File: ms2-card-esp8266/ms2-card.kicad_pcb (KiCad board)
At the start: 2 copper layers, 100 x 54 mm, 56 parts, among them J1 Schaltregler, J10 MicroSD_SPI_CD, J11 Conn_01x06, J2 ESP Prog, J20 Smartcard Connector, J21 PogoPin, J22 Card Edge, J23 Conn_01x04, J30 USB_B_Micro, J31 Power Select, J32 Conn_01x03, Q1 MMBT3904, Q2 MMBT3904, SW1 RESET, U1 ESP-12F, U2 FM24C64B, U20 BL1551B, U3 BL1551B, U30 CP2102N-Axx-xQFN24, U4 BL1551B, U6 AMS1117-3.3

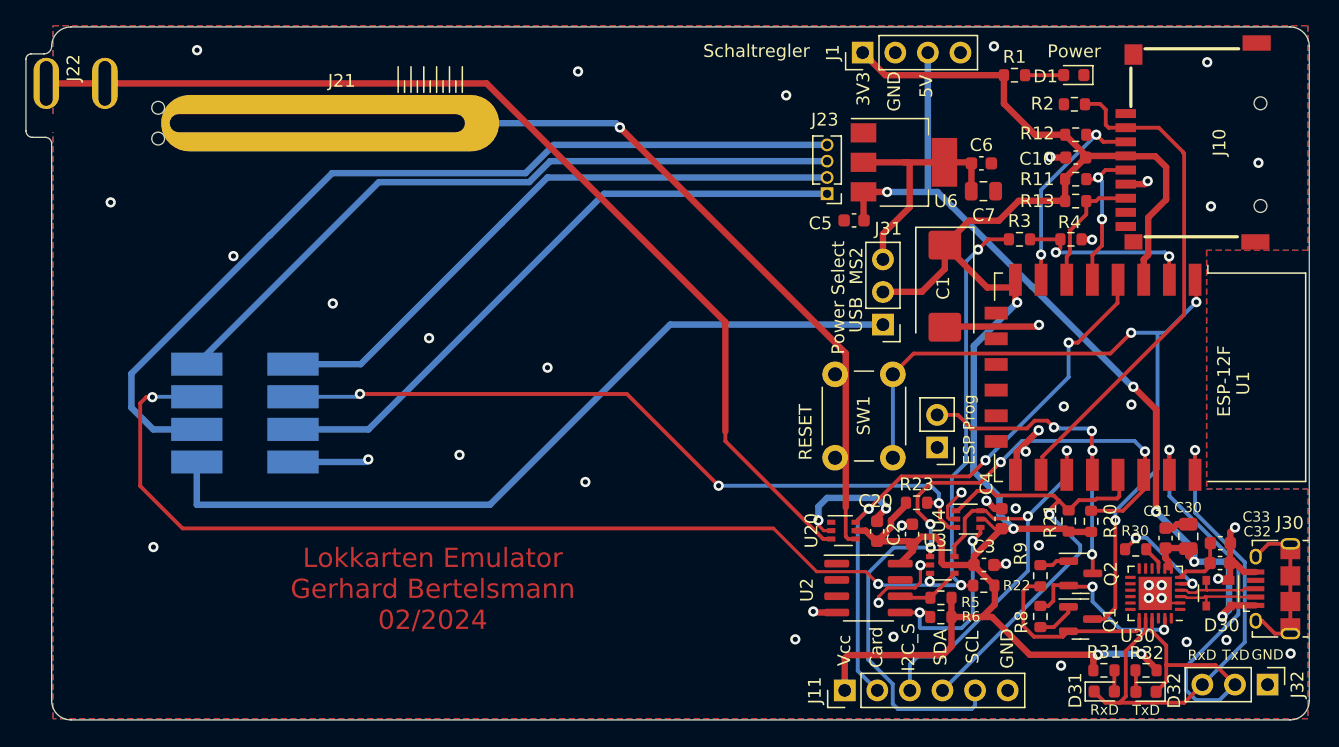
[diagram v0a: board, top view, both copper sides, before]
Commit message: add RC ADC oart
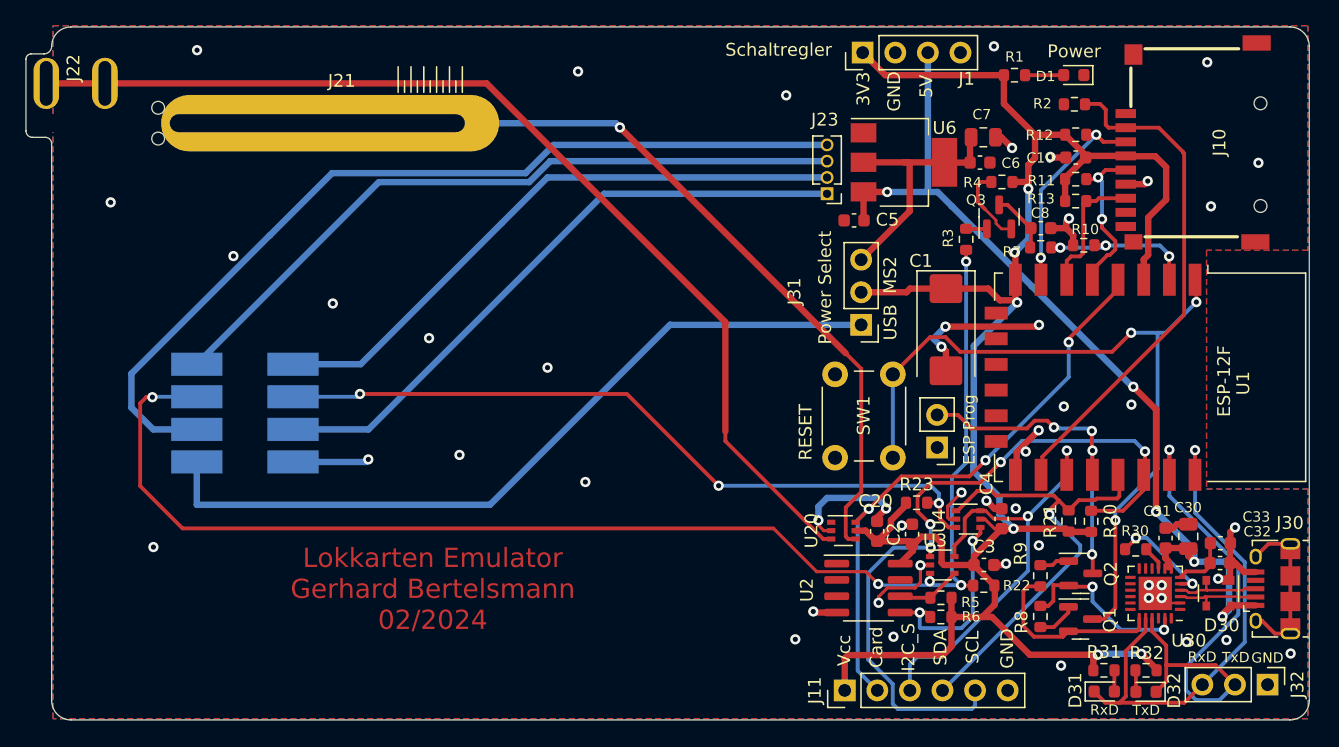
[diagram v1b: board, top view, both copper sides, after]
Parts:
- added C8: 470nF, Capacitor_SMD:C_0603_1608Metric, F.Cu at (177.1, 115.7)
- added Q3: MMBT5401, Package_TO_SOT_SMD:SOT-23, F.Cu at (173.8, 114.8)
- added R10: 75k, Resistor_SMD:R_0603_1608Metric, F.Cu at (180.4, 117.0)
- added R7: 180k, Resistor_SMD:R_0603_1608Metric, F.Cu at (177.1, 117.2)
- R3: value 220K -> 10k
- R4: value 100K -> 100
- moved R4 6.99 mm to (174.1, 112.1), turned to 0 degrees
- moved C7 4.20 mm to (172.6, 108.6)
- moved R3 4.16 mm to (171.3, 116.5), turned to -90 degrees
- moved C1 3.39 mm to (169.7, 123.6)
- moved J31 1.70 mm to (163.1, 123.2)
- moved C6 0.13 mm to (172.3, 110.6)
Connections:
- R3 pad 1: /CSCL -> Net-(Q3-Pad1)
- R3 pad 2: Net-(U1-Pad2) -> /CSCL
- R4 pad 1: GND -> Net-(Q3-Pad2)
- R4 pad 2: Net-(U1-Pad2) -> VCC
- U1 pad 2: Net-(U1-Pad2) -> /ADC
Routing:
- net Net-(U1-Pad2): track 14.3 -> 0.00 mm, vias 2 -> 0
- net /ADC: track 0.00 -> 12.4 mm, vias 0 -> 3
- net GND: track 56.9 -> 65.4 mm, vias 47 -> 50
- net Net-(Q3-Pad2): track 0.00 -> 6.11 mm
- net Net-(C8-Pad1): track 0.00 -> 4.75 mm
- net /CSCL: track 110.2 -> 107.1 mm
- net /MS2PWR: track 62.6 -> 60.9 mm
- net Net-(Q3-Pad1): track 0.00 -> 1.63 mm
- net /PP: track 63.7 -> 64.7 mm
- net /CLK: track 11.8 -> 12.8 mm
- net VCC: track 158.9 -> 159.9 mm, vias 4 -> 6
- net /nRST: track 59.3 -> 60.2 mm

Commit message: some small fixes
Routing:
- net GND: vias 50 -> 63
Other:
- board text added: "Lokkarten Emulator Gerhard Bertelsmann 03/2024"
- board text removed: "Lokkarten Emulator Gerhard Bertelsmann 02/2024"
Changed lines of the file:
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@@
   (title_block
     (title "Lokkkarten Emulator")
-    (date "2024-02-22")
-    (rev "0.96")
+    (date "2024-02-25")
+    (rev "0.98")
     (comment 1 "Gerhard Bertelsmann")
   )
@@
     (property "Sheetname" "")
     (attr smd)
-    (fp_text reference "C2" (at 0 -1.43 90) (layer "F.SilkS")
-      (effects (font (size 1 1) (thickness 0.15)))
+    (fp_text reference "C2" (at -0.545 -1.24 90) (layer "F.SilkS")
+      (effects (font (size 0.8 0.8) (thickness 0.15)))
     )
     (fp_text value "100nF" (at 0 1.43 90) (layer "F.Fab") hide
@@
     (property "Sheetname" "")
     (attr smd)
-    (fp_text reference "C20" (at 2.35 -0.125 180) (layer "F.SilkS")
-      (effects (font (size 1 1) (thickness 0.15)))
+    (fp_text reference "C20" (at 2.59 0.055 270) (layer "F.SilkS")
+      (effects (font (size 0.8 0.8) (thickness 0.15)))
     )
     (fp_text value "100nF" (at 0 1.43 90) (layer "F.Fab") hide
@@
     (property "Sheetname" "")
     (attr smd)
-    (fp_text reference "U3" (at -0.56 -1.905 180) (layer "F.SilkS")
-      (effects (font (size 1 1) (thickness 0.15)))
+    (fp_text reference "U3" (at -0.55 -2.015 180) (layer "F.SilkS")
+      (effects (font (size 0.8 0.8) (thickness 0.15)))
     )
     (fp_text value "BL1551B" (at 2.75 0 90) (layer "F.Fab") hide
@@
     (property "Sheetname" "")
     (attr smd)
-    (fp_text reference "U4" (at -2.275 0.14 90) (layer "F.SilkS")
-      (effects (font (size 1 1) (thickness 0.15)))
+    (fp_text reference "U4" (at 0.435 -1.86 180) (layer "F.SilkS")
+      (effects (font (size 0.8 0.8) (thickness 0.15)))
     )
     (fp_text value "BL1551B" (at 0 2 180) (layer "F.Fab") hide
@@
     (property "Sheetname" "")
     (attr smd)
-    (fp_text reference "C4" (at 2.745 -1.175 90) (layer "F.SilkS")
-      (effects (font (size 1 1) (thickness 0.15)))
+    (fp_text reference "C4" (at -0.015 1.525 90) (layer "F.SilkS")
+      (effects (font (size 0.8 0.8) (thickness 0.15)))
     )
     (fp_text value "100nF" (at 0 1.43 90) (layer "F.Fab") hide
@@
     (property "Sheetname" "")
     (attr smd)
-    (fp_text reference "C3" (at 0 -1.43) (layer "F.SilkS")
-      (effects (font (size 1 1) (thickness 0.15)))
+    (fp_text reference "C3" (at 0.15 -1.245) (layer "F.SilkS")
+      (effects (font (size 0.8 0.8) (thickness 0.15)))
     )
     (fp_text value "100nF" (at 0 1.43) (layer "F.Fab") hide
@@
   (gr_arc (start 100 101.5) (mid 100.43934 100.43934) (end 101.5 100) (layer "Edge.Cuts") (width 0.05))
   (gr_arc (start 196.5 100) (mid 197.56066 100.43934) (end 198 101.5) (layer "Edge.Cuts") (width 0.05))
-  (gr_text "Lokkarten Emulator\nGerhard Bertelsmann\n02/2024" (at 129.7 143.8) (layer "F.Cu")
+  (gr_text "Lokkarten Emulator\nGerhard Bertelsmann\n03/2024" (at 129.7 143.8) (layer "F.Cu")
     (effects (font (size 1.5 1.5) (thickness 0.3)))
   )
-  (gr_text "SCL" (at 171.76 148.34 90) (layer "F.SilkS")
+  (gr_text "SCL" (at 172.07 148.71 90) (layer "F.SilkS")
     (effects (font (size 1 1) (thickness 0.15)))
   )
-  (gr_text "GND" (at 174.46 148.44 90) (layer "F.SilkS")
+  (gr_text "GND" (at 174.53 148.63 90) (layer "F.SilkS")
     (effects (font (size 1 1) (thickness 0.15)))
   )
@@
     (effects (font (size 1 1) (thickness 0.15)))
   )
-  (gr_text "Vcc" (at 161.76 148.59 90) (layer "F.SilkS")
+  (gr_text "Vcc" (at 161.83 148.94 90) (layer "F.SilkS")
     (effects (font (size 1 1) (thickness 0.15)))
   )
@@
     (effects (font (size 0.8 0.8) (thickness 0.15)))
   )
-  (gr_text "SDA" (at 169.26 148.34 90) (layer "F.SilkS")
+  (gr_text "SDA" (at 169.49 148.77 90) (layer "F.SilkS")
     (effects (font (size 1 1) (thickness 0.15)))
   )
@@
     (effects (font (size 0.8 0.8) (thickness 0.15)))
   )
-  (gr_text "I2C_S" (at 166.76 148.34 90) (layer "F.SilkS")
+  (gr_text "I2C_S" (at 166.94 148.35 90) (layer "F.SilkS")
     (effects (font (size 1 1) (thickness 0.15)))
   )
-  (gr_text "Card" (at 164.26 148.34 90) (layer "F.SilkS")
+  (gr_text "Card" (at 164.4 148.51 90) (layer "F.SilkS")
     (effects (font (size 1 1) (thickness 0.15)))
   )
@@
   (segment (start 160.175 139.25) (end 159.75 138.825) (width 0.25) (layer "F.Cu") (net 2))
   (segment (start 179.605 116.225) (end 179.605 117.01) (width 0.5) (layer "F.Cu") (net 2))
-  (via (at 185.5 143.5) (size 0.8) (drill 0.4) (layers "F.Cu" "B.Cu") (net 2))
+  (via (at 185.41 143.55) (size 0.8) (drill 0.4) (layers "F.Cu" "B.Cu") (net 2))
+  (via (at 183.29 104.5) (size 0.8) (drill 0.4) (layers "F.Cu" "B.Cu") (free) (net 2))
   (via (at 172.8454 136.918398) (size 0.8) (drill 0.4) (layers "F.Cu" "B.Cu") (net 2))
   (via (at 175.91 133.09) (size 0.8) (drill 0.4) (layers "F.Cu" "B.Cu") (free) (net 2))
   (via (at 166.25 138.85) (size 0.8) (drill 0.4) (layers "F.Cu" "B.Cu") (net 2))
+  (via (at 166.61 123.09) (size 0.8) (drill 0.4) (layers "F.Cu" "B.Cu") (free) (net 2))
   (via (at 141.02 103.47) (size 0.8) (drill 0.4) (layers "F.Cu" "B.Cu") (free) (net 2))
   (via (at 169.65 123.35) (size 0.8) (drill 0.4) (layers "F.Cu" "B.Cu") (net 2))
-  (via (at 185.5 144.5) (size 0.8) (drill 0.4) (layers "F.Cu" "B.Cu") (net 2))
+  (via (at 164.7 130.33) (size 0.8) (drill 0.4) (layers "F.Cu" "B.Cu") (free) (net 2))
+  (via (at 185.37 144.77) (size 0.8) (drill 0.4) (layers "F.Cu" "B.Cu") (net 2))
+  (via (at 169.49 118.02) (size 0.8) (drill 0.4) (layers "F.Cu" "B.Cu") (free) (net 2))
   (via (at 185.411812 112.011812) (size 0.8) (drill 0.4) (layers "F.Cu" "B.Cu") (net 2))
   (via (at 167.6995 141.95) (size 0.8) (drill 0.4) (layers "F.Cu" "B.Cu") (net 2))
@@
   (via (at 169.34 124.92) (size 0.8) (drill 0.4) (layers "F.Cu" "B.Cu") (net 2))
   (via (at 121.91 121.55) (size 0.8) (drill 0.4) (layers "F.Cu" "B.Cu") (free) (net 2))
+  (via (at 176.27 127.51) (size 0.8) (drill 0.4) (layers "F.Cu" "B.Cu") (free) (net 2))
+  (via (at 173.25 149.38) (size 0.8) (drill 0.4) (layers "F.Cu" "B.Cu") (free) (net 2))
   (via (at 176.93 140.4) (size 0.8) (drill 0.4) (layers "F.Cu" "B.Cu") (net 2))
   (via (at 177.825 110.125) (size 0.8) (drill 0.4) (layers "F.Cu" "B.Cu") (net 2))
@@
   (via (at 178.875 129.575) (size 0.8) (drill 0.4) (layers "F.Cu" "B.Cu") (net 2))
   (via (at 196.55 148.825) (size 0.8) (drill 0.4) (layers "F.Cu" "B.Cu") (free) (net 2))
+  (via (at 149.06 141.37) (size 0.8) (drill 0.4) (layers "F.Cu" "B.Cu") (free) (net 2))
   (via (at 190.34 113.98) (size 0.8) (drill 0.4) (layers "F.Cu" "B.Cu") (free) (net 2))
   (via (at 159.75 138.45) (size 0.8) (drill 0.4) (layers "F.Cu" "B.Cu") (net 2))
+  (via (at 170.77 106.06) (size 0.8) (drill 0.4) (layers "F.Cu" "B.Cu") (free) (net 2))
   (via (at 138.64 126.55) (size 0.8) (drill 0.4) (layers "F.Cu" "B.Cu") (free) (net 2))
   (via (at 114.164312 117.854312) (size 0.8) (drill 0.4) (layers "F.Cu" "B.Cu") (free) (net 2))
   (via (at 124.675 133.7) (size 0.8) (drill 0.4) (layers "F.Cu" "B.Cu") (net 2))
   (via (at 190.9005 142.996083) (size 0.8) (drill 0.4) (layers "F.Cu" "B.Cu") (net 2))
+  (via (at 183.95 125.47) (size 0.8) (drill 0.4) (layers "F.Cu" "B.Cu") (free) (net 2))
+  (via (at 117.34 118.43) (size 0.8) (drill 0.4) (layers "F.Cu" "B.Cu") (free) (net 2))
   (via (at 178.657792 149.7695) (size 0.8) (drill 0.4) (layers "F.Cu" "B.Cu") (free) (net 2))
+  (via (at 167.38 116.81) (size 0.8) (drill 0.4) (layers "F.Cu" "B.Cu") (free) (net 2))
   (via (at 184.14 129.43) (size 0.8) (drill 0.4) (layers "F.Cu" "B.Cu") (net 2))
+  (via (at 181.98 101.15) (size 0.8) (drill 0.4) (layers "F.Cu" "B.Cu") (free) (net 2))
+  (via (at 183.37 122.21) (size 0.8) (drill 0.4) (layers "F.Cu" "B.Cu") (free) (net 2))
   (via (at 165.025 137.525) (size 0.8) (drill 0.4) (layers "F.Cu" "B.Cu") (net 2))
   (via (at 174.84 109.43) (size 0.8) (drill 0.4) (layers "F.Cu" "B.Cu") (net 2))
@@
   (via (at 174.375 141.825) (size 0.8) (drill 0.4) (layers "F.Cu" "B.Cu") (net 2))
   (via (at 131.78 133.35) (size 0.8) (drill 0.4) (layers "F.Cu" "B.Cu") (free) (net 2))
-  (via (at 186.5 144.5) (size 0.8) (drill 0.4) (layers "F.Cu" "B.Cu") (net 2))
+  (via (at 186.63 144.79) (size 0.8) (drill 0.4) (layers "F.Cu" "B.Cu") (net 2))
   (via (at 141.59 135.46) (size 0.8) (drill 0.4) (layers "F.Cu" "B.Cu") (free) (net 2))
-  (via (at 186.5 143.5) (size 0.8) (drill 0.4) (layers "F.Cu" "B.Cu") (net 2))
+  (via (at 186.6 143.54) (size 0.8) (drill 0.4) (layers "F.Cu" "B.Cu") (net 2))
   (via (at 165.6 147.52) (size 0.8) (drill 0.4) (layers "F.Cu" "B.Cu") (free) (net 2))
   (via (at 188.45 147.925) (size 0.8) (drill 0.4) (layers "F.Cu" "B.Cu") (free) (net 2))

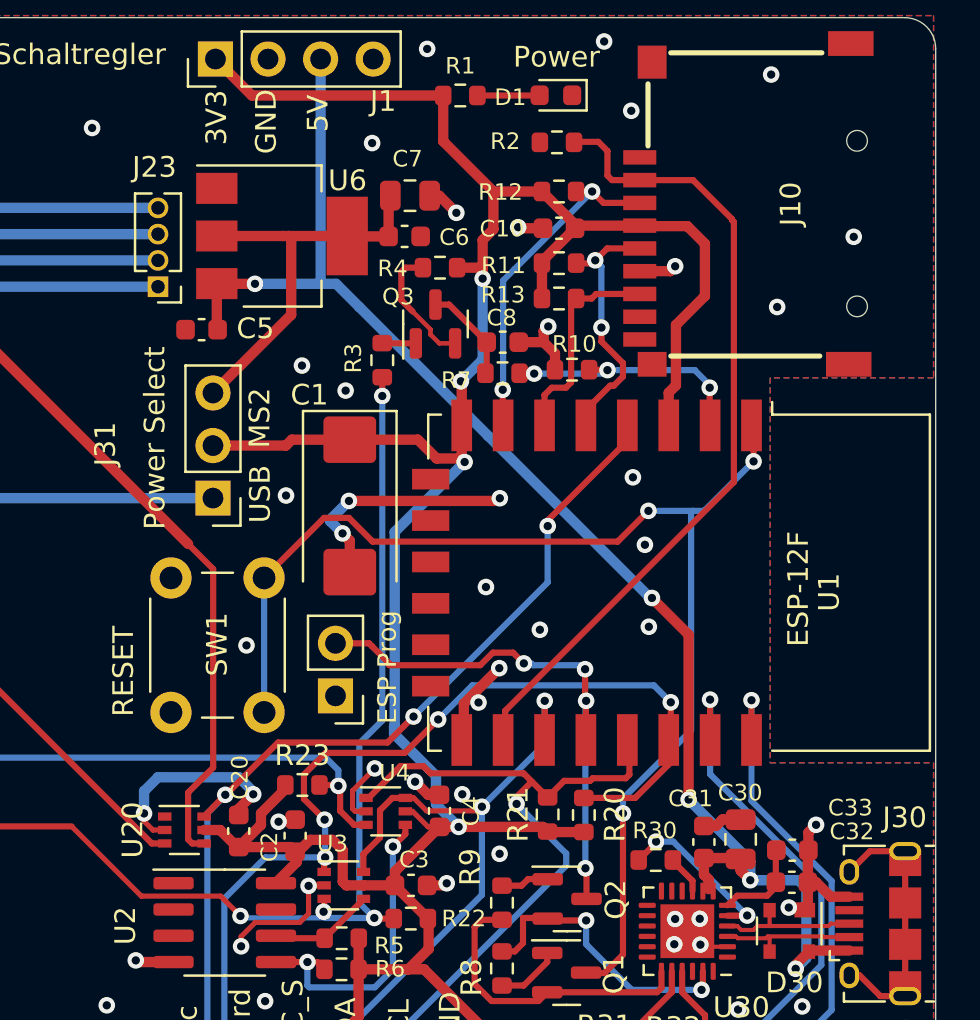
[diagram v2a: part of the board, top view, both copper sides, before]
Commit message: pull up unused SD card IO pins
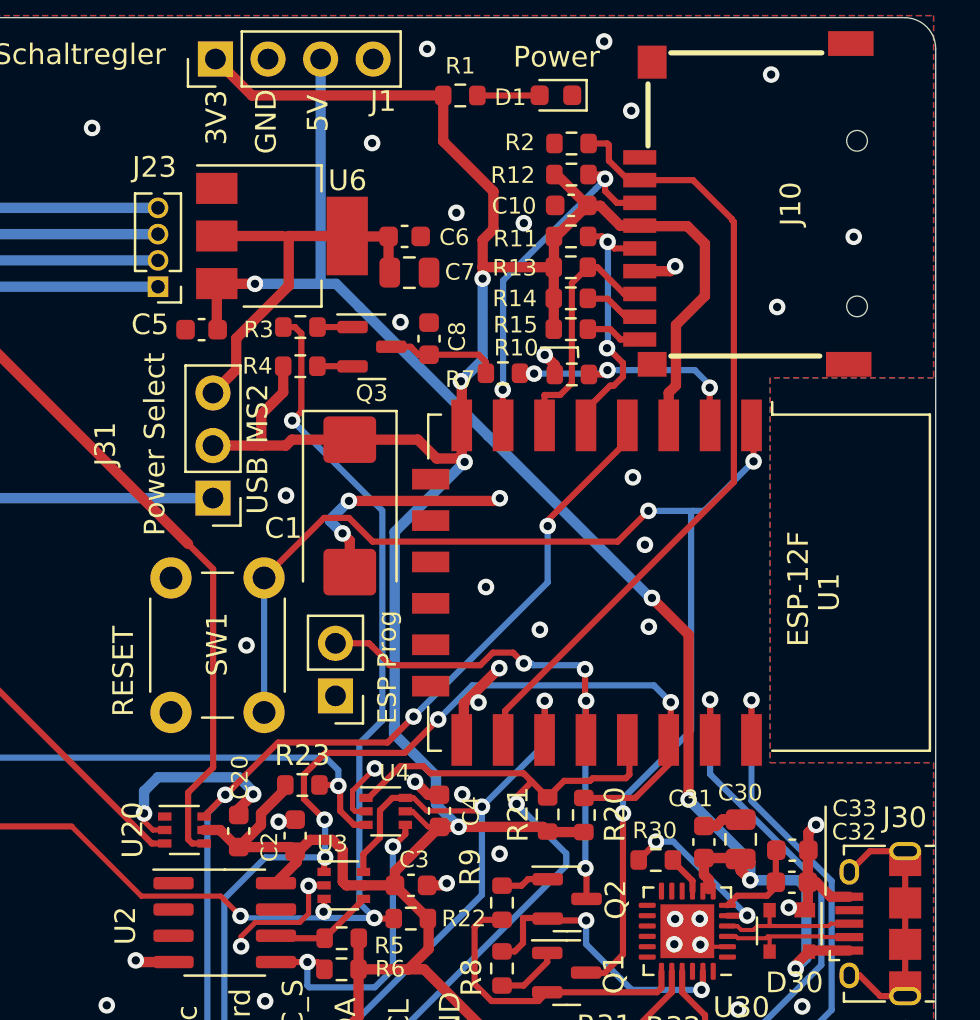
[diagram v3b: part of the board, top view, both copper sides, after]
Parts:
- added R14: 4k7, Resistor_SMD:R_0603_1608Metric, F.Cu at (180.4, 113.6)
- added R15: 4k7, Resistor_SMD:R_0603_1608Metric, F.Cu at (180.4, 115.0)
- moved R4 8.26 mm to (167.3, 116.8), turned to 180 degrees
- moved R3 4.27 mm to (167.3, 115.0), turned to 180 degrees
- moved C7 3.72 mm to (172.6, 112.3)
- moved C8 3.56 mm to (173.5, 115.5), turned to 90 degrees
- moved Q3 3.26 mm to (170.8, 115.9), turned to 0 degrees
- moved R13 1.61 mm to (180.4, 112.1)
- moved R11 1.41 mm to (180.4, 110.6)
- moved C10 1.25 mm to (180.4, 109.1)
- moved R12 1.02 mm to (180.4, 107.6)
- moved R2 0.71 mm to (180.4, 106.1)
- moved R10 0.23 mm to (180.4, 117.2)
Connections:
- J10 pad 8: unconnected-(J10-Pad8) -> /DAT1
- J10 pad 9: unconnected-(J10-Pad9) -> /DAT2
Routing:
- net VCC: track 159.9 -> 166.2 mm
- net GND: track 65.4 -> 60.1 mm, vias 63 -> 62
- net /CSCL: track 107.1 -> 112.2 mm
- net Net-(Q3-Pad2): track 6.11 -> 1.70 mm
- net /DAT1: track 0.00 -> 2.87 mm
- net /DAT2: track 0.00 -> 2.72 mm
- net /MISO: track 10.3 -> 12.0 mm
- net /CS: track 39.1 -> 38.1 mm
- net /MOSI: track 16.4 -> 17.4 mm
- net Net-(C8-Pad1): track 4.75 -> 5.41 mm
- net +3V3: track 19.5 -> 18.9 mm
